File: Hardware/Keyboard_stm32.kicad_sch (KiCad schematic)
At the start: 30 parts, among them IC1 TS02-66-80-BK-160-LCR-D, IC2 TPA6102A2DGKR, U1 STM32F072C8Tx, Y1 16 MHz

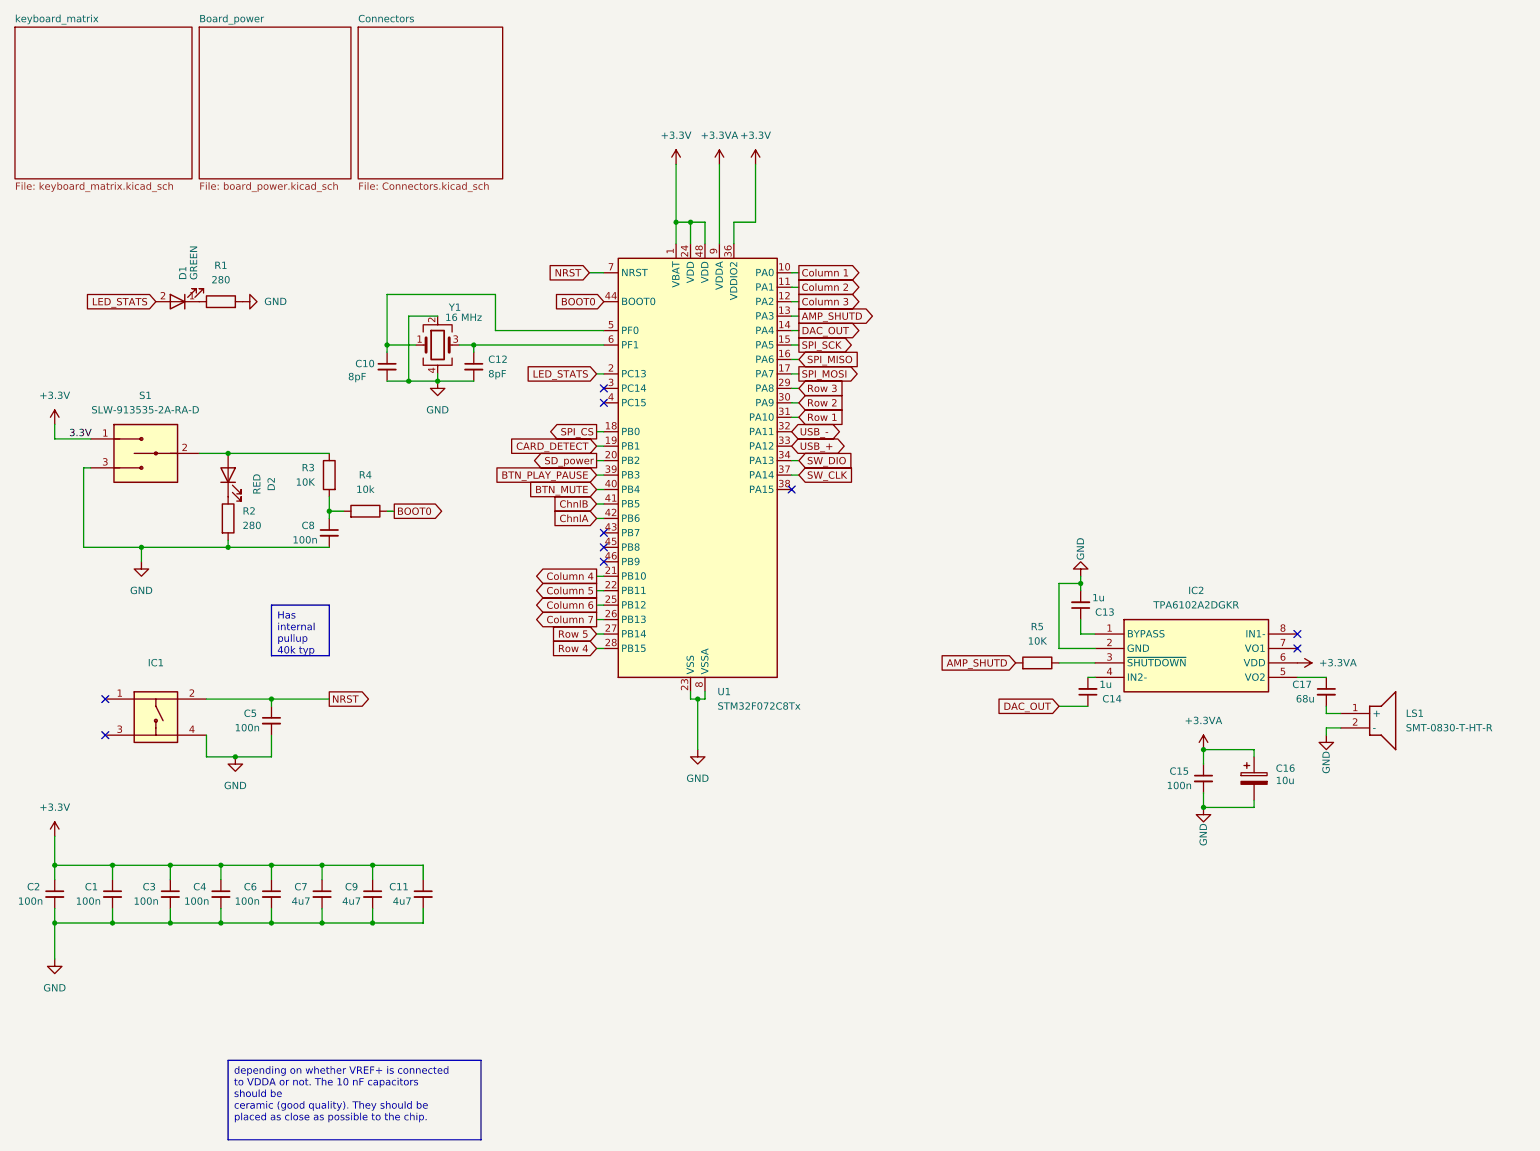
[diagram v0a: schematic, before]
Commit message: updated files, added PDF versions on schematic and PCB
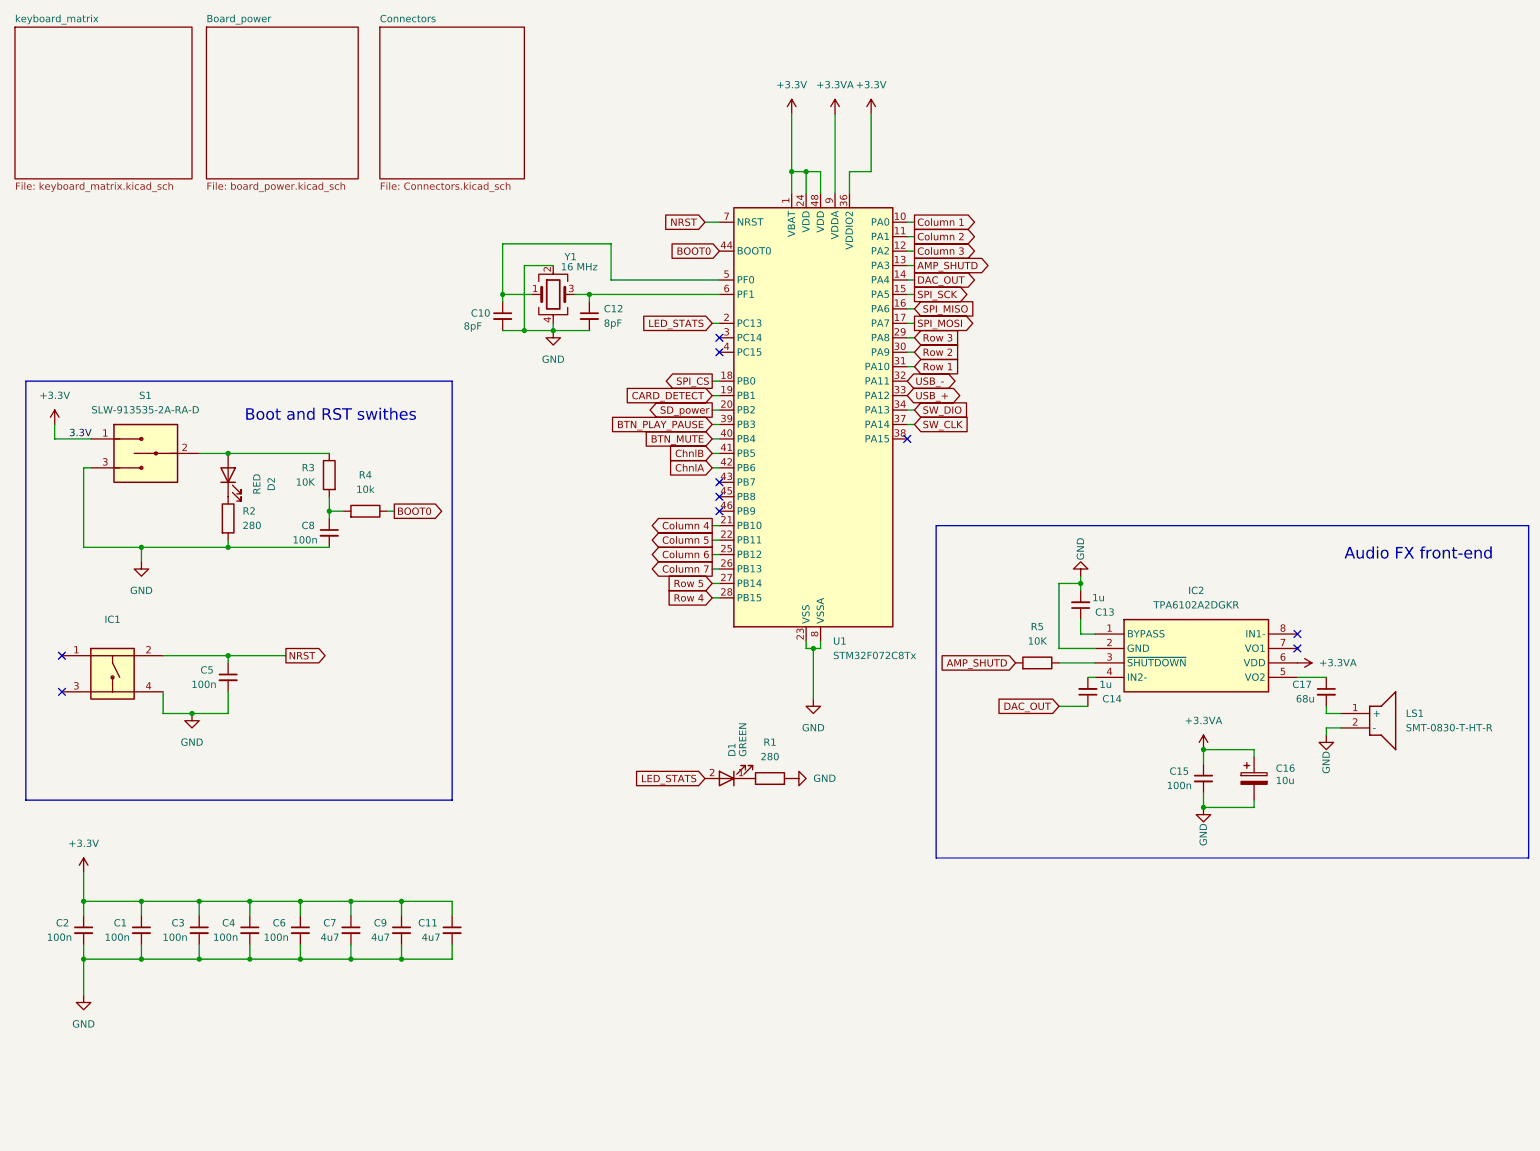
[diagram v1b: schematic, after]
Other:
- note added: "Audio FX front-end"
- note added: "Boot and RST swithes"
- moved on the sheet: C1, C10, C11, C12, C2, C3, C4, C5, C6, C7, C9, D1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
